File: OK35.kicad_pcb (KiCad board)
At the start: 2 copper layers, 133.3 x 116.2 mm, 78 parts, among them SW1 SW_SPST, SW10 SW_SPST, SW11 SW_SPST, SW12 SW_SPST, SW13 SW_SPST, SW14 SW_SPST, SW15 SW_SPST, SW16 SW_SPST, SW17 SW_SPST, SW18 SW_SPST, SW19 SW_SPST, SW2 SW_SPST, SW20 SW_SPST, SW21 SW_SPST, SW22 SW_SPST, SW23 SW_SPST, SW24 SW_SPST, SW25 SW_SPST, SW26 SW_SPST, SW27 SW_SPST, SW28 SW_SPST, SW29 SW_SPST, SW3 SW_SPST, SW30 SW_SPST, SW31 SW_SPST, SW32 SW_SPST, SW33 SW_SPST, SW34 SW_SPST, SW35 SW_SPST, SW4 SW_SPST, SW5 SW_SPST, SW6 SW_SPST, SW7 SW_SPST, SW8 SW_SPST, SW9 SW_SPST, U1 TRRS, U2 ProMicro

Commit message: Add files via upload
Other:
- board text added: "CC-BY-SA moth.monster"
- board text removed: "35 keyswitches of your choice 35 1N4148 diodes 2 220Ω resistors 1 PJ-320A TRRS jack 1 Pro Micro-compatible microcontroller"
- board text removed: "Be careful what you say online. It will never truly be forgotten. CC-BY-SA moth.monster"
- board text removed: "INGREDIENTS:"
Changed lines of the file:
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@@
   (gr_line (start 136.525 -5.08) (end 3.175 -5.08) (layer "Edge.Cuts") (width 0.1))
   (gr_line (start 136.525 111.125) (end 136.525 -5.08) (layer "Edge.Cuts") (width 0.1))
-  (gr_text "INGREDIENTS:" (at 57.15 -0.635 90) (layer "F.SilkS")
-    (effects (font (size 1 0.75) (thickness 0.15)))
-  )
-  (gr_text "Be careful what you say online.\nIt will never truly be forgotten.\n\nCC-BY-SA moth.monster" (at 41.275 0) (layer "F.SilkS")
+  (gr_text "CC-BY-SA moth.monster" (at 41.275 2.54) (layer "F.SilkS")
     (effects (font (size 1 1) (thickness 0.15)))
   )
@@
     (effects (font (size 1 1) (thickness 0.15)) (justify left))
   )
-  (gr_text "35 keyswitches of your choice\n35 1N4148 diodes\n2 220Ω resistors\n1 PJ-320A TRRS jack\n1 Pro Micro-compatible microcontroller" (at 58.42 -0.635) (layer "F.SilkS")
-    (effects (font (size 1 1) (thickness 0.15)) (justify left))
-  )

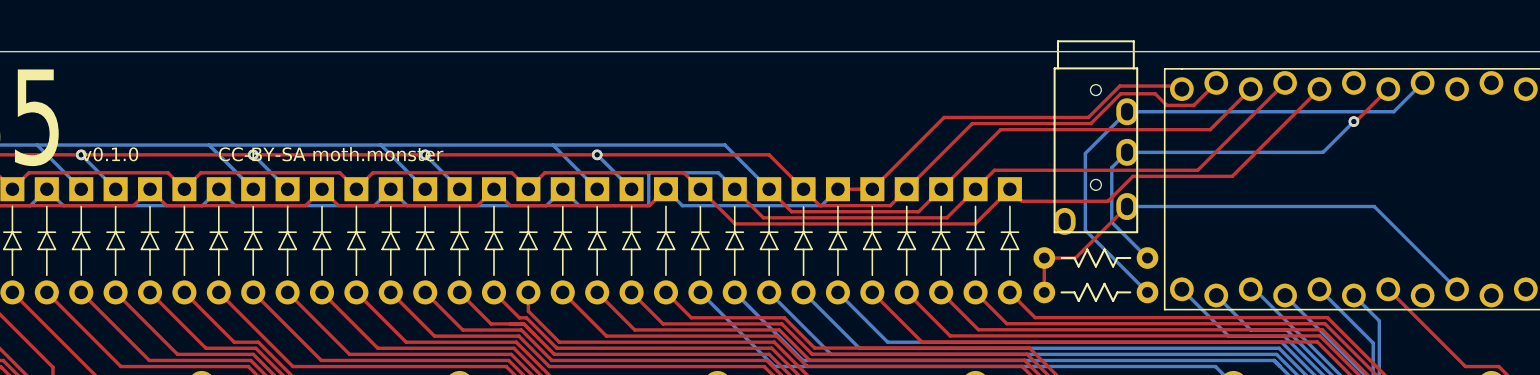
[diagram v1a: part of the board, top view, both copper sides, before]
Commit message: v0.1.1 - fixing noob mistakes
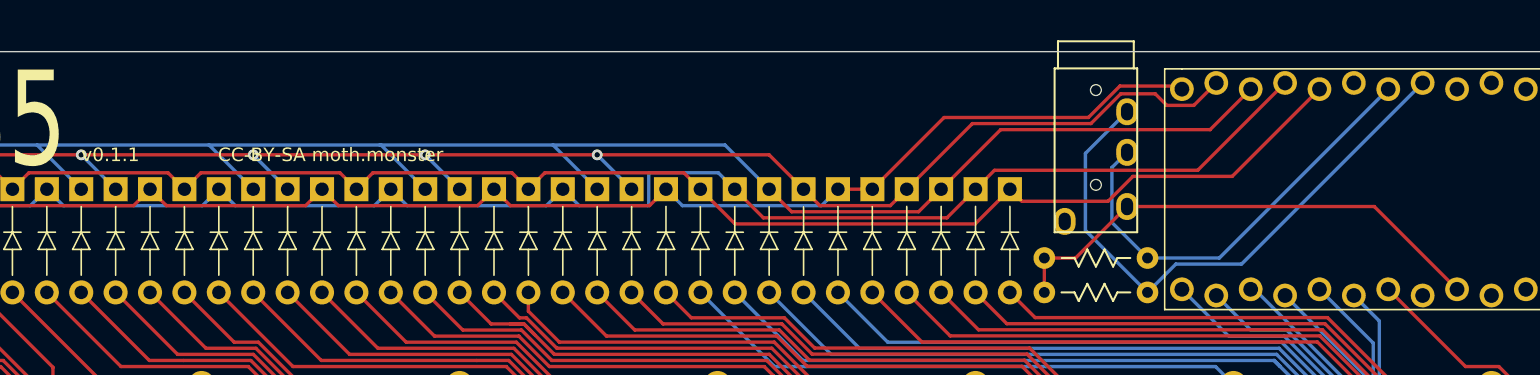
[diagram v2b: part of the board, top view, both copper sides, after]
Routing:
- net SDA: track 39.2 -> 43.2 mm
- net SCL: track 30.6 -> 32.3 mm, vias 1 -> 0
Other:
- board text added: "v0.1.1"
- board text removed: "v0.1.0"
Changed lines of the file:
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@@
     (effects (font (size 1 1) (thickness 0.15)))
   )
-  (gr_text "v0.1.0" (at 22.86 2.54) (layer "F.SilkS")
+  (gr_text "v0.1.1" (at 22.86 2.54) (layer "F.SilkS")
     (effects (font (size 1 1) (thickness 0.15)) (justify left))
   )
@@
   (segment (start 120.015 36.195) (end 118.926919 37.283081) (width 0.25) (layer "F.Cu") (net 40))
   (segment (start 118.926919 87.626919) (end 127 95.7) (width 0.25) (layer "F.Cu") (net 40))
-  (segment (start 119.7939 -0.6425) (end 121.92 -2.7686) (width 0.25) (layer "B.Cu") (net 41))
   (segment (start 100.09 -0.6425) (end 97.015479 2.432021) (width 0.25) (layer "B.Cu") (net 41))
-  (segment (start 100.09 -0.6425) (end 119.7939 -0.6425) (width 0.25) (layer "B.Cu") (net 41))
   (segment (start 97.015479 8.115479) (end 101.6 12.7) (width 0.25) (layer "B.Cu") (net 41))
+  (segment (start 101.6 12.7) (end 103.69048 10.60952) (width 0.25) (layer "B.Cu") (net 41))
+  (segment (start 108.54188 10.60952) (end 121.92 -2.7686) (width 0.25) (layer "B.Cu") (net 41))
+  (segment (start 103.69048 10.60952) (end 108.54188 10.60952) (width 0.25) (layer "B.Cu") (net 41))
   (segment (start 97.015479 2.432021) (end 97.015479 8.115479) (width 0.25) (layer "B.Cu") (net 41))
   (segment (start 96.2875 10.16) (end 100.09 6.3575) (width 0.25) (layer "F.Cu") (net 42))
   (segment (start 93.98 12.7) (end 93.98 10.16) (width 0.25) (layer "F.Cu") (net 42))
   (segment (start 93.98 10.16) (end 96.2875 10.16) (width 0.25) (layer "F.Cu") (net 42))
-  (segment (start 100.09 6.3575) (end 118.3461 6.3575) (width 0.25) (layer "B.Cu") (net 42))
-  (segment (start 118.3461 6.3575) (end 124.46 12.4714) (width 0.25) (layer "B.Cu") (net 42))
-  (segment (start 116.84 0.082) (end 116.9866 0.082) (width 0.25) (layer "F.Cu") (net 43))
-  (segment (start 116.9866 0.082) (end 119.38 -2.3114) (width 0.25) (layer "F.Cu") (net 43))
-  (via (at 116.84 0.082) (size 0.8) (drill 0.4) (layers "F.Cu" "B.Cu") (net 43))
-  (segment (start 114.5645 2.3575) (end 116.84 0.082) (width 0.25) (layer "B.Cu") (net 43))
+  (segment (start 100.09 6.3575) (end 118.3461 6.3575) (width 0.25) (layer "F.Cu") (net 42))
+  (segment (start 118.3461 6.3575) (end 124.46 12.4714) (width 0.25) (layer "F.Cu") (net 42))
   (segment (start 100.09 2.3575) (end 98.96548 3.48202) (width 0.25) (layer "B.Cu") (net 43))
   (segment (start 98.96548 7.52548) (end 101.6 10.16) (width 0.25) (layer "B.Cu") (net 43))
-  (segment (start 100.09 2.3575) (end 114.5645 2.3575) (width 0.25) (layer "B.Cu") (net 43))
+  (segment (start 101.6 10.16) (end 106.9086 10.16) (width 0.25) (layer "B.Cu") (net 43))
   (segment (start 98.96548 3.48202) (end 98.96548 7.52548) (width 0.25) (layer "B.Cu") (net 43))
+  (segment (start 106.9086 10.16) (end 119.38 -2.3114) (width 0.25) (layer "B.Cu") (net 43))
   (segment (start 15.9 40.65) (end 15.2 39.95) (width 0.25) (layer "F.Cu") (net 44))
   (segment (start 17.7 21.6) (end 15.9 21.6) (width 0.25) (layer "F.Cu") (net 44))

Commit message: cleanup some stuff
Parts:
- moved R1 85.0 mm to (177.8, 50.4)
- moved R2 85.0 mm to (177.8, 47.8)
- moved REF** 85.0 mm to (193.7, 72.6)
- moved SW18 85.0 mm to (146.1, 101.2)
- moved SW25 85.0 mm to (146.1, 120.2)
- moved SW32 85.0 mm to (146.1, 139.2)
- moved D1 85.0 mm to (86.4, 46.5)
- moved D11 85.0 mm to (127.0, 46.5)
- moved D13 85.0 mm to (152.4, 46.5)
- moved D14 85.0 mm to (170.2, 46.5)
- moved D15 85.0 mm to (91.4, 46.5)
- moved D16 85.0 mm to (104.1, 46.5)
- moved D17 85.0 mm to (116.8, 46.5)
- moved D19 85.0 mm to (142.2, 46.5)
- moved D2 85.0 mm to (99.1, 46.5)
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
